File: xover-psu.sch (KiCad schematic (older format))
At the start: 97 parts, among them J1 Screw_Terminal_01x02, J2 Screw_Terminal_01x02, J3 Screw_Terminal_01x02, J4 Screw_Terminal_01x02, J5 Screw_Terminal_01x03, J6 Screw_Terminal_01x02, J7 Screw_Terminal_01x02, J8 Screw_Terminal_01x03, K1 T9GS5L14-12, Q1 AO3400, Q2 2N7002, Q3 AO3400, U1 817C, U2 TL431LP, U3 LM317_3PinPackage, U4 LM337_TO220, U5 TL431LP, U6 817C

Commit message: improved TL431 biasing, higher-ESR filter cap options for stability
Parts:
- added C24, C25: 10u, Capacitors_SMD:C_0805, symbol Device:C
- added R12: 15k, Resistors_SMD:R_0805, symbol Device:R
- added R13: 10k, Resistors_SMD:R_0805, symbol Device:R
- added R21: 1k, Resistors_SMD:R_0805, symbol Device:R
- added R25, R26: 1, Resistors_SMD:R_0805, symbol Device:R
- C15, C16: value 10u -> 100n
- C20, C21: value 10u -> 22u; footprint Capacitors_SMD:C_0805 -> Capacitors_SMD:C_1210_HandSoldering
- C22, C23: value 10u -> 22u; footprint Capacitors_SMD:C_0805 -> Capacitors_ThroughHole:CP_Radial_Tantal_D6.0mm_P5.00mm
- F1, F2: footprint (none) -> Fuse_Holders_and_Fuses:Fuseholder5x20_horiz_open_universal_Type-III
- R9: renamed from R11; value 10k -> 3k9
- renumbered D18 to D16, D16 to D17, D17 to D18, R9 to R10, R10 to R11, R12 to R14, R13 to R15, R14 to R16, R15 to R17, R16 to R19, R17 to R20, R19 to R22, R20 to R23, R21 to R24, R22 to R27, R23 to R28, R24 to R29, R25 to R30, R26 to R31
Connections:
- wire segments 327 -> 343
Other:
- moved on the sheet: C17, D17, D18, D19, D20, J8, Q2, R14, R18, R30, R31, R9

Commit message: defined all the custom footprints
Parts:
- K1: value T9GS5L14-12 -> T9GS1L14-12; footprint (none) -> power:Potter_T9G_Relay
- L1: footprint (none) -> power:PM3700
- PS1: footprint Converter_ACDC:Converter_ACDC_HiLink_HLK-PMxx -> power:HLK-10M12
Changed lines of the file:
@@
 	1750 3700 2000 3700
 Connection ~ 1750 3700
-$Comp
-L Converter_ACDC:HLK-PM12 PS1
-U 1 1 6164FFC7
-P 3750 6450
-F 0 "PS1" H 3750 6775 50  0000 C CNN
-F 1 "HLK-10M12" H 3750 6684 50  0000 C CNN
-F 2 "Converter_ACDC:Converter_ACDC_HiLink_HLK-PMxx" H 3750 6150 50  0001 C CNN
-F 3 "http://www.hlktech.net/product_detail.php?ProId=56" H 4150 6100 50  0001 C CNN
-	1    3750 6450
-	1    0    0    -1
-$EndComp
-$Comp
-L Device:L_Coupled L1
-U 1 1 616524A0
-P 2950 6450
-F 0 "L1" H 2950 6731 50  0000 C CNN
-F 1 "PM3700_70_RC" H 2950 6300 50  0000 C CNN
-F 2 "" H 2950 6450 50  0001 C CNN
-F 3 "~" H 2950 6450 50  0001 C CNN
-	1    2950 6450
-	1    0    0    -1
-$EndComp
 Wire Wire Line
 	3150 6350 3350 6350
@@
 P 2150 4350
 F 0 "K1" V 1583 4350 50  0000 C CNN
-F 1 "T9GS5L14-12" V 1674 4350 50  0000 C CNN
-F 2 "" H 2600 4300 50  0001 L CNN
+F 1 "T9GS1L14-12" V 1674 4350 50  0000 C CNN
+F 2 "power:Potter_T9G_Relay" H 2600 4300 50  0001 L CNN
 F 3 "https://a3.sofastcdn.com/attachment/7jioKBjnRiiSrjrjknRiwS77gwbf3zmp/L90-SERIES.pdf" H 2800 4200 50  0001 L CNN
 	1    2150 4350
@@
 Connection ~ 9200 5700
 Connection ~ 9000 5700
+$Comp
+L Converter_ACDC:HLK-PM12 PS1
+U 1 1 6164FFC7
+P 3750 6450
+F 0 "PS1" H 3750 6775 50  0000 C CNN
+F 1 "HLK-10M12" H 3750 6684 50  0000 C CNN
+F 2 "power:HLK-10M12" H 3750 6150 50  0001 C CNN
+F 3 "http://www.hlktech.net/product_detail.php?ProId=56" H 4150 6100 50  0001 C CNN
+	1    3750 6450
+	1    0    0    -1
+$EndComp
+$Comp
+L Device:L_Coupled L1
+U 1 1 616524A0
+P 2950 6450
+F 0 "L1" H 2950 6731 50  0000 C CNN
+F 1 "PM3700_70_RC" H 2950 6150 50  0000 C CNN
+F 2 "power:PM3700" H 2950 6450 50  0001 C CNN
+F 3 "~" H 2950 6450 50  0001 C CNN
+	1    2950 6450
+	1    0    0    1
+$EndComp
 $EndSCHEMATC

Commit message: Completed placement (no routing) on layout
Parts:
- removed C10, C11, C12, C13, C14, C9: 1000u, Capacitors_ThroughHole:CP_Radial_D16.0mm_P7.50mm, symbol Device:CP
- removed C17, C24, C25: 10u, Capacitors_SMD:C_0805, symbol Device:C
- removed C3: 220u, Capacitors_SMD:CP_Elec_10x10, symbol Device:C
- removed JP1, JP3: Jumper_2_Open, Terminal_Blocks:TerminalBlock_bornier-2_P5.08mm, symbol Jumper:Jumper_2_Open
- removed JP2: Jumper_2_Bridged, Terminal_Blocks:TerminalBlock_bornier-2_P5.08mm, symbol Jumper:Jumper_2_Bridged
- removed R25, R26: 1, Resistors_SMD:R_0805, symbol Device:R
- removed U2, U5: TL431LP, Package_TO_SOT_THT:TO-92_Inline, symbol Reference_Voltage:TL431LP
- added C17, C3: 220u, Capacitors_SMD:CP_Elec_10x10, symbol Device:CP
- added U2, U6: TL431DBZ, TO_SOT_Packages_SMD:SOT-23, symbol Reference_Voltage:TL431DBZ
- C1, C2: MFG Name (none) -> Panasonic; MFG Part Num (none) -> ECQU2A104KLA
- C18, C19: footprint Capacitors_SMD:C_0805 -> Capacitors_SMD:C_1210
- C4: value 1u -> 10u; footprint Capacitors_SMD:C_0805 -> Capacitors_SMD:C_1210
- C5, C6, C7, C8: value 1000u -> 3300u; footprint Capacitors_ThroughHole:CP_Radial_D16.0mm_P7.50mm -> smd:CP_Elec_EEEFK-K16
- J1, J2, J3, J4, J6, J7: footprint Terminals_Phoenix:TerminalBlock_Phoenix_MPT-2.54mm_2pol -> Terminals_Phoenix:TerminalBlock_Phoenix_MKDS1.5-2pol
- L1: MFG Name (none) -> Bourns
- R14: value 1k -> 100
- R15: value 270k -> 27k
- R18: value 100k -> 10k
- R6, R7, R8: value 47k -> 4k7
- U1: footprint Package_DIP:DIP-4_W7.62mm -> Housings_DIP:DIP-4_W7.62mm_Socket
- U5: renamed from U4; footprint Package_TO_SOT_THT:TO-220-3_Vertical -> TO_SOT_Packages_THT:TO-220-3_Vertical
- U8: renamed from U6; footprint Package_DIP:DIP-4_W7.62mm -> Housings_DIP:DIP-4_W7.62mm_Socket
- renumbered K1 to K2, R12 to R10, R10 to R11, R11 to R12, U3 to U4
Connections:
- net labels added: RECT2
- wire segments 343 -> 349
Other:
- moved on the sheet: C4, D1, D10, D2, D3, D5, D6, D7, D8, D9, J2, J3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

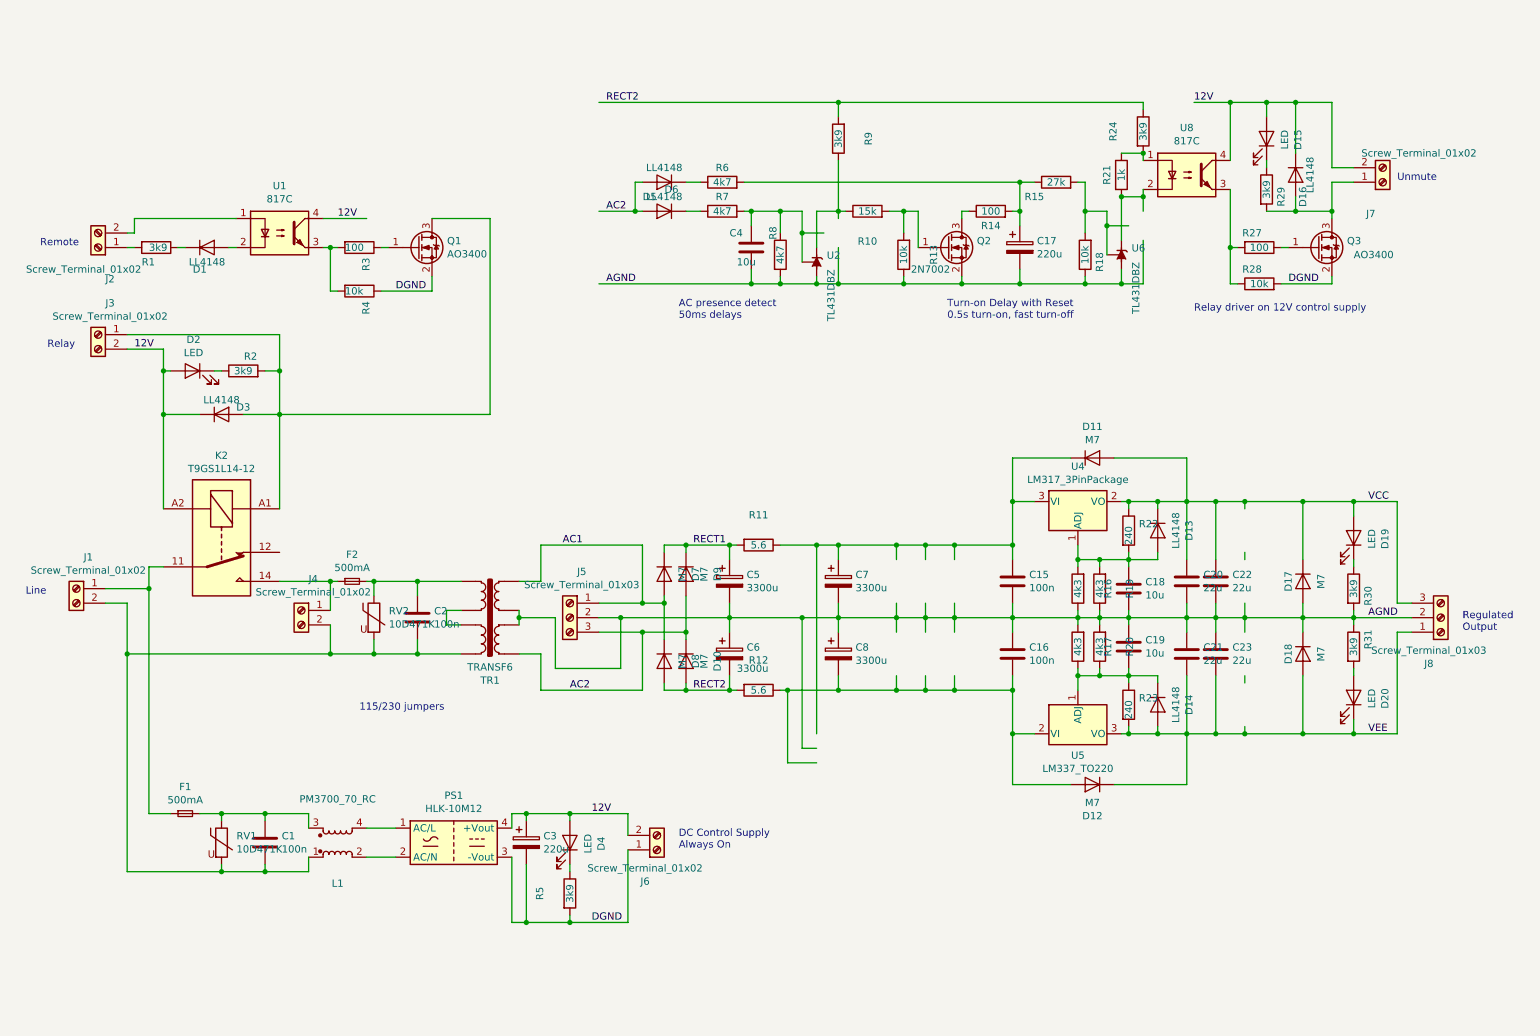
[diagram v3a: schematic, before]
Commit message: First pass routing completed for all but the UNMUTE timer/logic
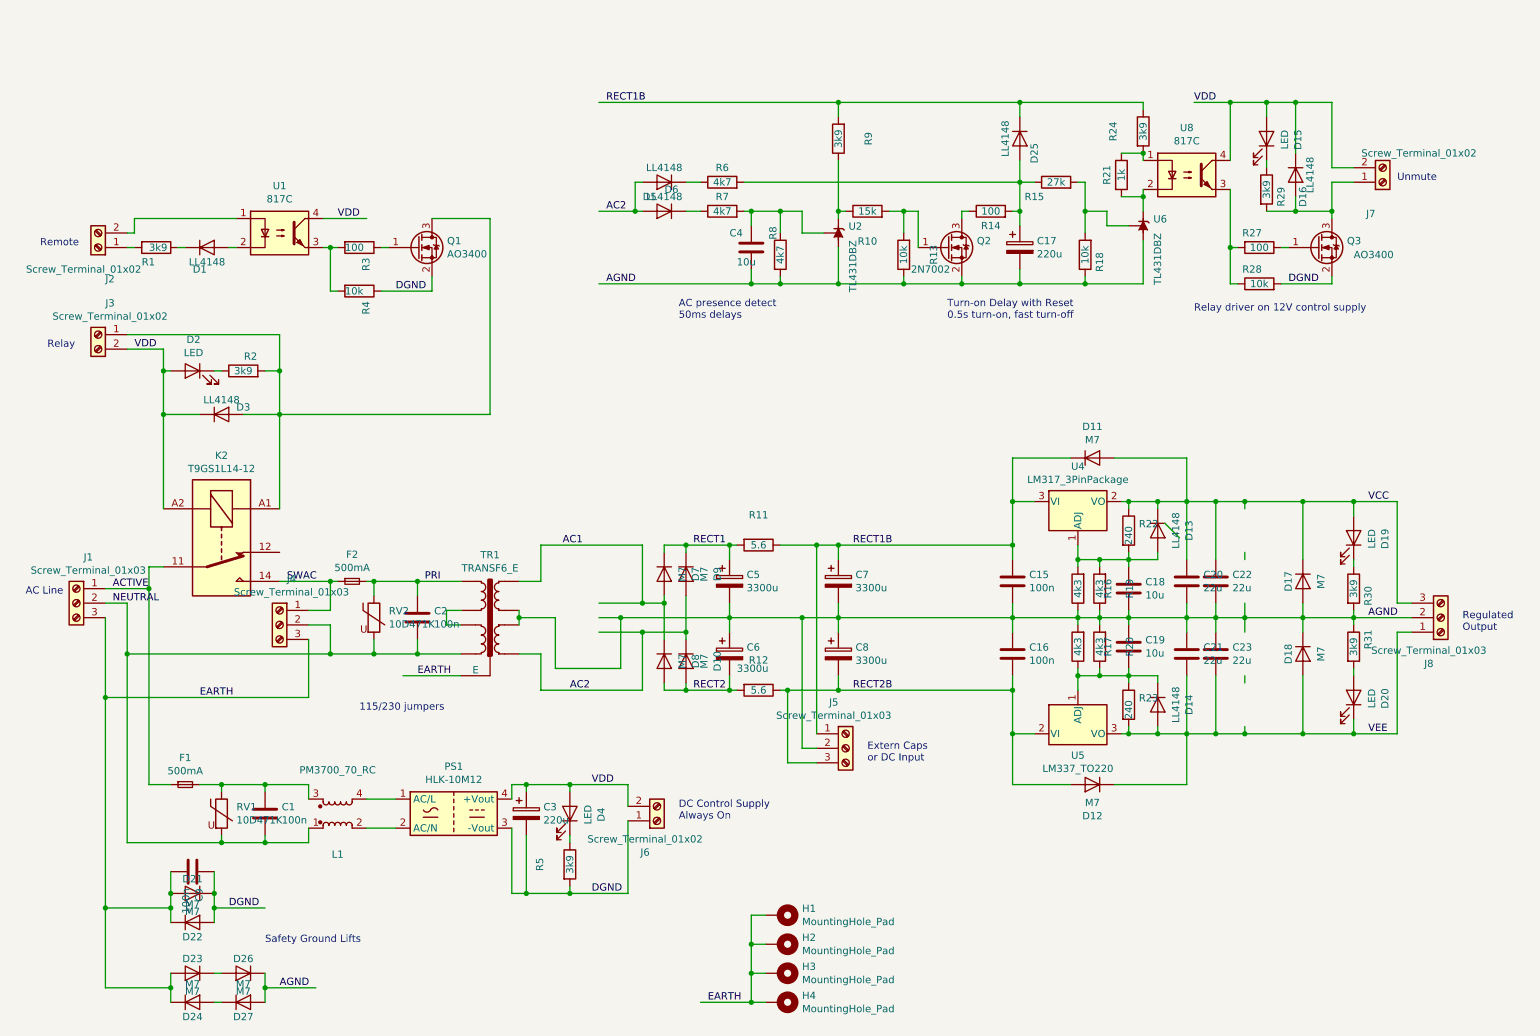
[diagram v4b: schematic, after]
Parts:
- removed J1, J4: Screw_Terminal_01x02, Terminals_Phoenix:TerminalBlock_Phoenix_MKDS1.5-2pol, symbol Connector:Screw_Terminal_01x02
- removed TR1: TRANSF6, pcb:Trafo_CHK-EI54-12VA_Combo, symbol Transformer:TRANSF6
- added C9: 100n, Capacitors_SMD:C_0805, symbol Device:C
- added D21, D22, D23, D24, D26, D27: M7, Diodes_SMD:D_SMA, symbol Device:D
- added D25: LL4148, Diodes_SMD:D_MiniMELF, symbol Device:D
- added H1, H2, H3, H4: MountingHole_Pad, Mounting_Holes:MountingHole_3.2mm_M3_DIN965_Pad, symbol Mechanical:MountingHole_Pad
- added J1, J4: Screw_Terminal_01x03, Terminals_Phoenix:TerminalBlock_Phoenix_MKDS1.5-3pol, symbol Connector:Screw_Terminal_01x03
- added TR1: TRANSF6_E, power:Trafo_CHK-EI54-12VA_Combo_Vigor, symbol wbt-device:TRANSF6_E
- F1, F2: footprint Fuse_Holders_and_Fuses:Fuseholder5x20_horiz_open_universal_Type-III -> power:Fuseholder5x20_6mm
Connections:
- net labels added: ACTIVE, EARTH, NEUTRAL, PRI, RECT1B, RECT2B, SWAC, VDD
- net labels removed: 12V
- wire segments 349 -> 354
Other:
- note added: "AC Line"
- note added: "Extern Caps\nor DC Input"
- note added: "Safety Ground Lifts"
- note removed: "Line"
- moved on the sheet: C1, C3, D4, F1, J5, J6, L1, PS1, R5, RV1, U2, U6

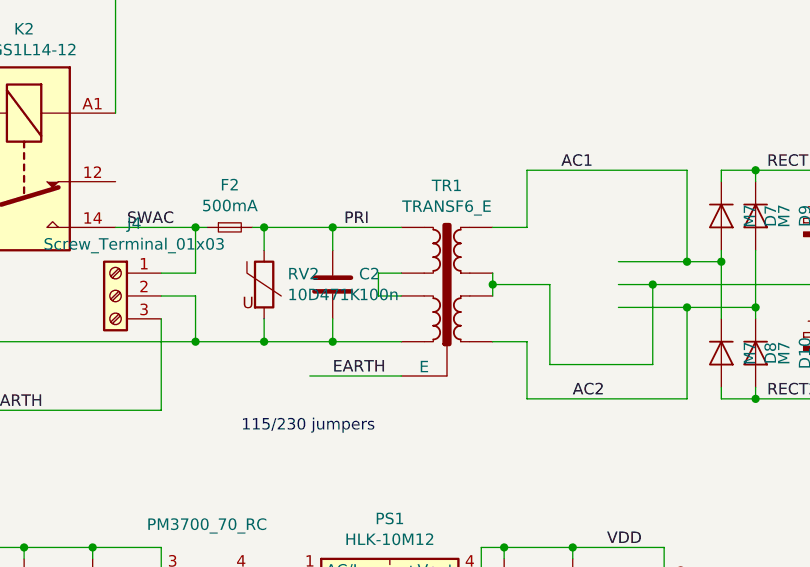
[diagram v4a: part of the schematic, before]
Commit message: Fixed transformer phase, made some mains tracks fatter
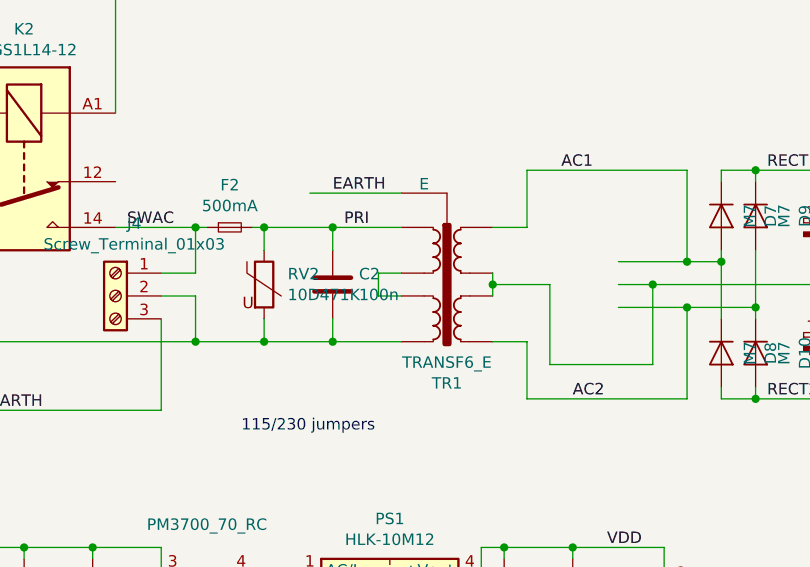
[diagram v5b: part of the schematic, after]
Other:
- moved on the sheet: TR1
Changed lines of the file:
@@
 L wbt-device:TRANSF6_E TR1
 U 1 1 6173240D
-P 4000 4850
-F 0 "TR1" H 4000 4468 50  0000 C CNN
-F 1 "TRANSF6_E" H 4000 4559 50  0000 C CNN
-F 2 "power:Trafo_CHK-EI54-12VA_Combo_Vigor" H 4000 4850 50  0001 C CNN
-F 3 "" H 4000 4850 50  0001 C CNN
-	1    4000 4850
-	1    0    0    1
+P 4000 4950
+F 0 "TR1" H 4000 4568 50  0000 C CNN
+F 1 "TRANSF6_E" H 4000 4659 50  0000 C CNN
+F 2 "power:Trafo_CHK-EI54-12VA_Combo_Vigor" H 4000 4950 50  0001 C CNN
+F 3 "" H 4000 4950 50  0001 C CNN
+	1    4000 4950
+	1    0    0    -1
 $EndComp
 Wire Wire Line
-	3800 5300 3400 5300
-Text Label 3500 5300 0    50   ~ 0
+	3800 4500 3400 4500
+Text Label 3500 4500 0    50   ~ 0
 EARTH
 $Comp

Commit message: prettified everything - round corners, readable silkscreens, etc.
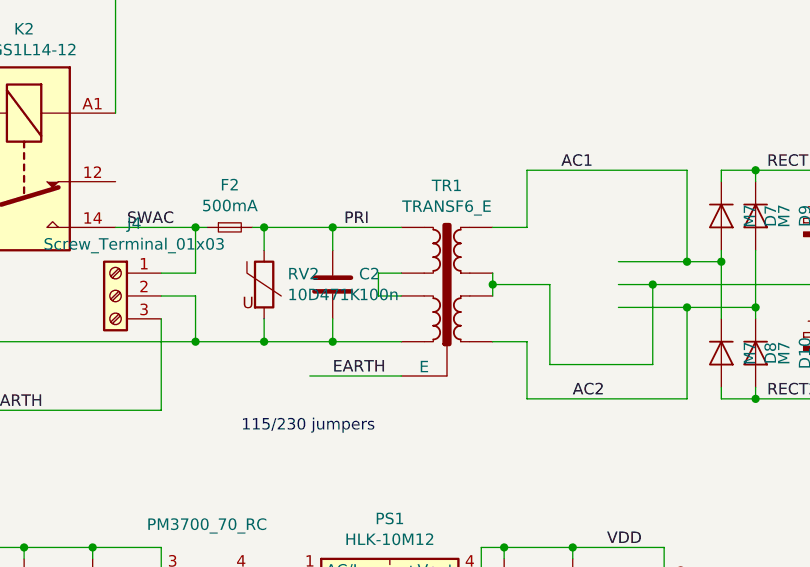
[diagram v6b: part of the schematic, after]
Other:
- moved on the sheet: TR1
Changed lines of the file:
@@
 L wbt-device:TRANSF6_E TR1
 U 1 1 6173240D
-P 4000 4950
-F 0 "TR1" H 4000 4568 50  0000 C CNN
-F 1 "TRANSF6_E" H 4000 4659 50  0000 C CNN
-F 2 "power:Trafo_CHK-EI54-12VA_Combo_Vigor" H 4000 4950 50  0001 C CNN
-F 3 "" H 4000 4950 50  0001 C CNN
-	1    4000 4950
-	1    0    0    -1
+P 4000 4850
+F 0 "TR1" H 4000 4468 50  0000 C CNN
+F 1 "TRANSF6_E" H 4000 4559 50  0000 C CNN
+F 2 "power:Trafo_CHK-EI54-12VA_Combo_Vigor" H 4000 4850 50  0001 C CNN
+F 3 "" H 4000 4850 50  0001 C CNN
+	1    4000 4850
+	1    0    0    1
 $EndComp
 Wire Wire Line
-	3800 4500 3400 4500
-Text Label 3500 4500 0    50   ~ 0
+	3800 5300 3400 5300
+Text Label 3500 5300 0    50   ~ 0
 EARTH
 $Comp
